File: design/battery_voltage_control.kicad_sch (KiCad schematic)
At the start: 12 parts

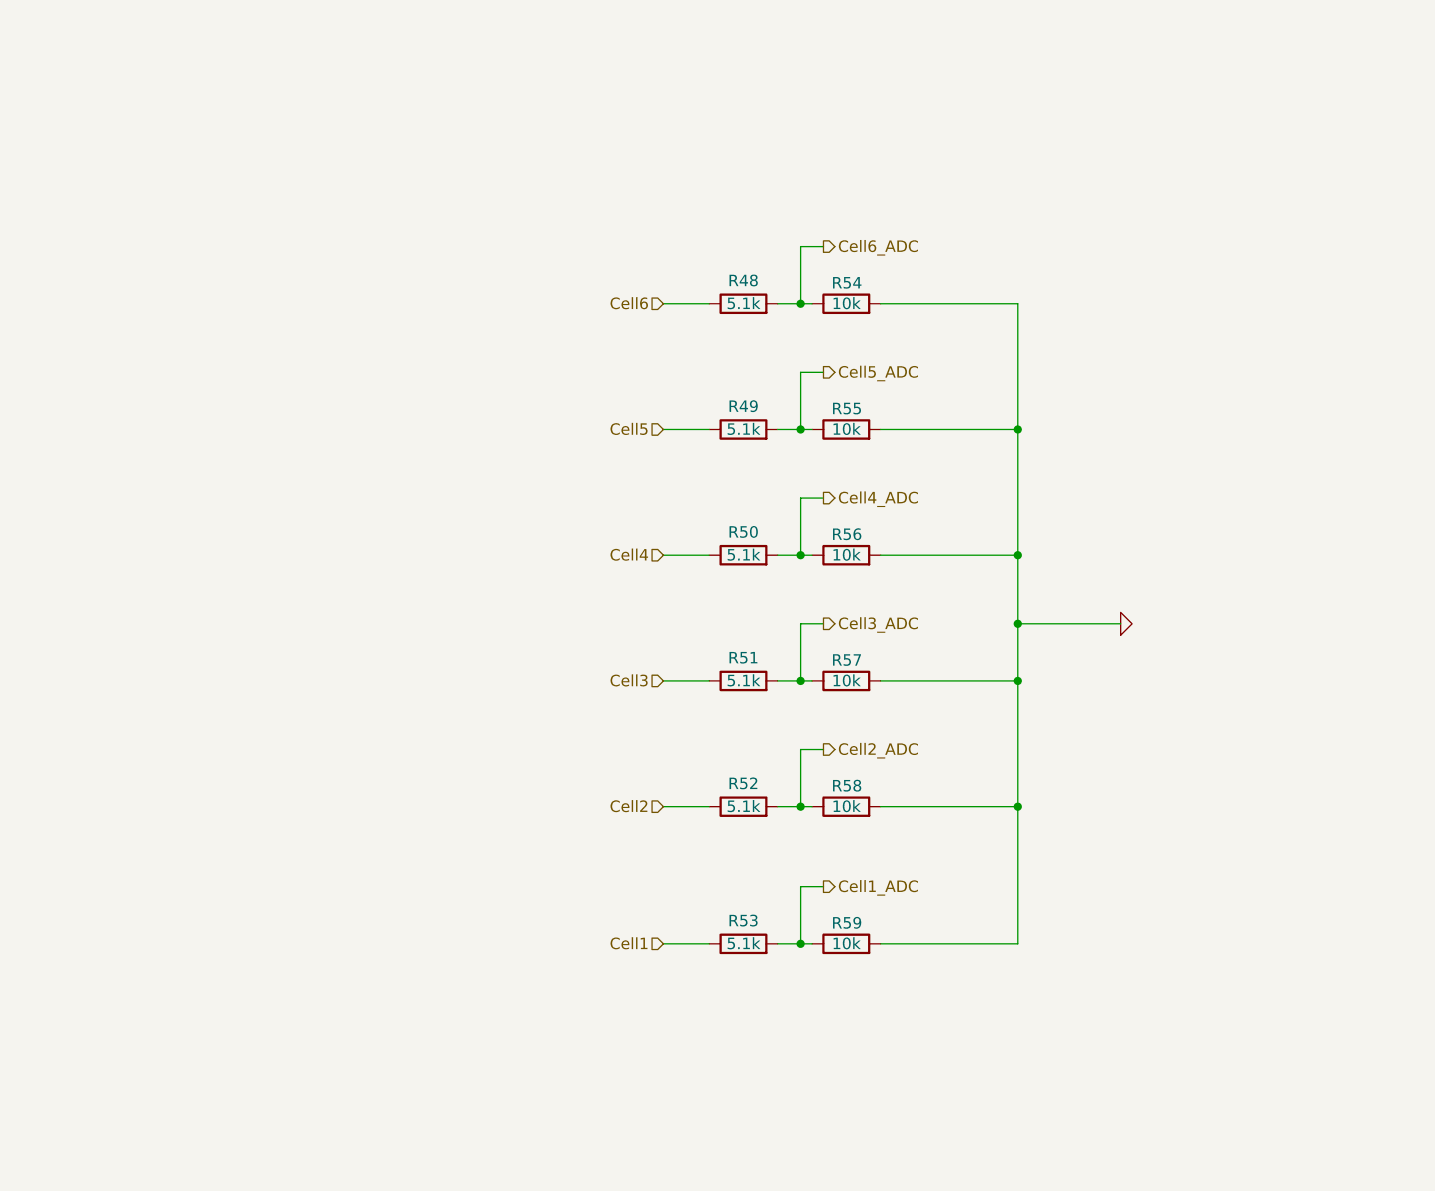
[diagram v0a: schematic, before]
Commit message: added battery balancer
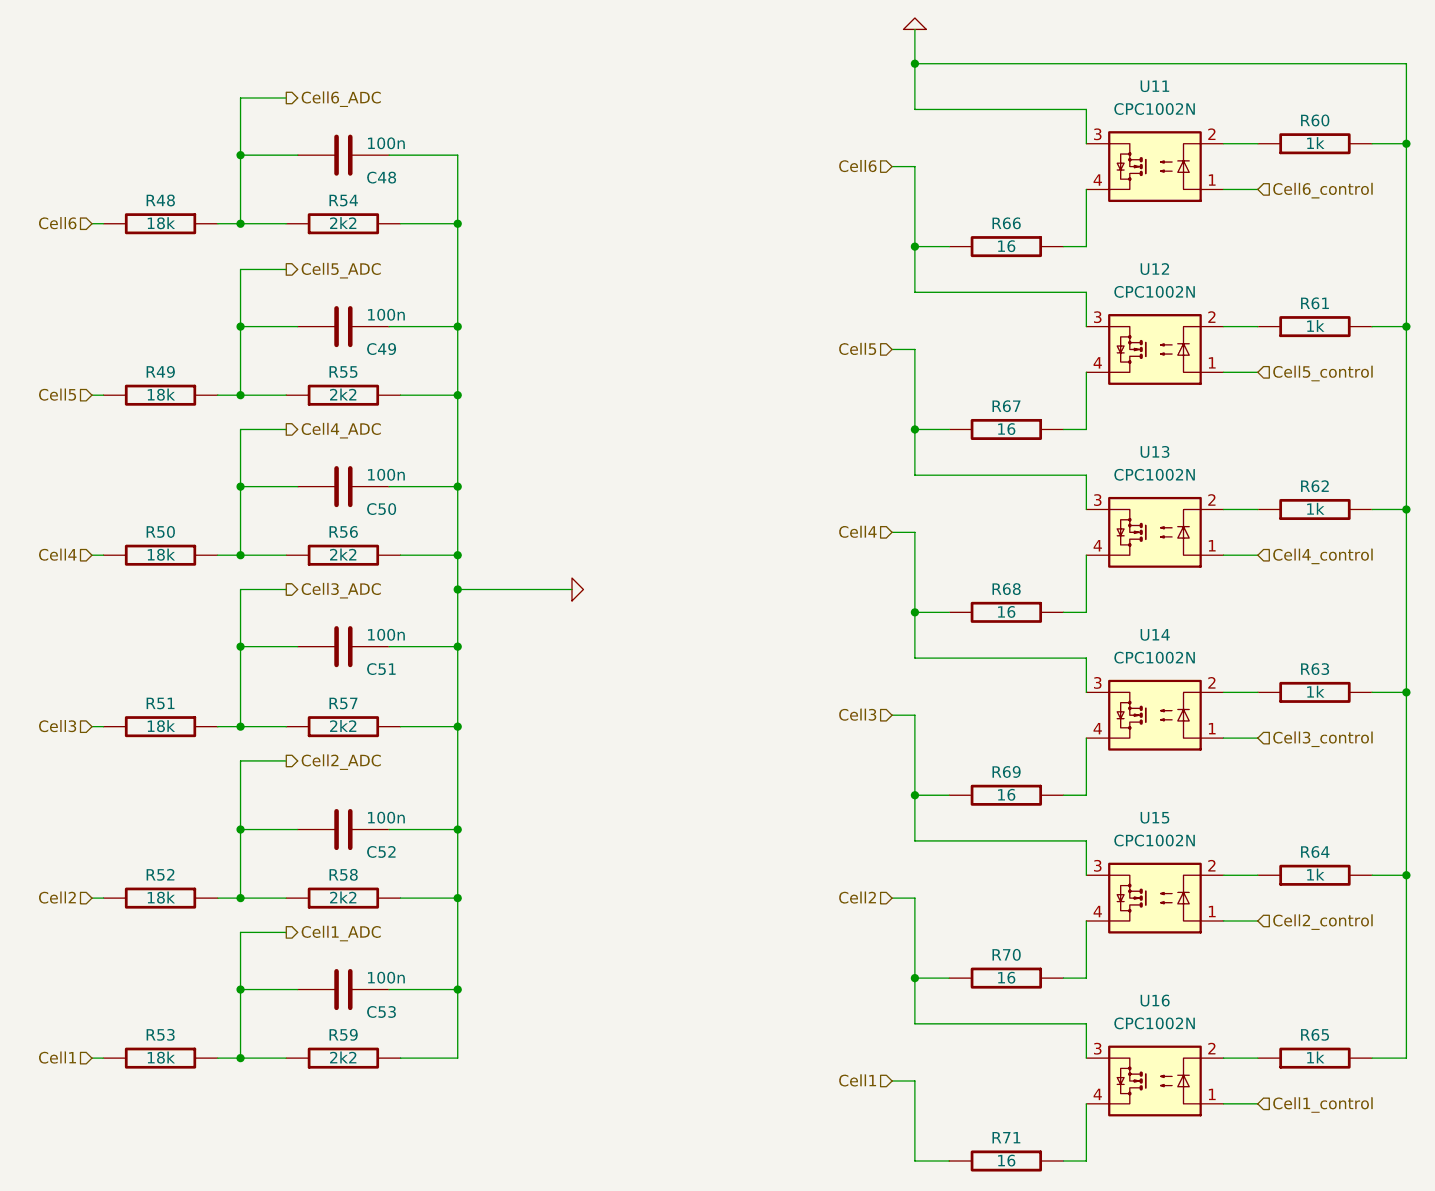
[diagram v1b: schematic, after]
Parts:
- removed R48, R49, R50, R51, R52, R53: 5.1k, CRF1:SMD-0603_r, symbol Device:R
- removed R54, R55, R56, R57, R58, R59: 10k, CRF1:SMD-0603_r, symbol Device:R
- added C48, C49, C50, C51, C52, C53: 100n, CRF1:SMD-0603_c, symbol BLDC_4-rescue:C-RESCUE-BLDC_4
- added R48, R49, R50, R51, R52, R53: 18k, CRF1:SMD-0603_r, symbol BLDC_4-rescue:R-RESCUE-BLDC_4
- added R54, R55, R56, R57, R58, R59: 2k2, CRF1:SMD-0603_r, symbol BLDC_4-rescue:R-RESCUE-BLDC_4
- added R60, R61, R62, R63, R64, R65: 1k, CRF1:SMD-0603_r, symbol BLDC_4-rescue:R-RESCUE-BLDC_4
- added R66, R67, R68, R69, R70, R71: 16, Resistor_SMD:R_2512_6332Metric, symbol BLDC_4-rescue:R-RESCUE-BLDC_4
- added U11, U12, U13, U14, U15, U16: CPC1002N, Package_SO:SOP-4_3.8x4.1mm_P2.54mm, symbol Relay_SolidState:CPC1002N
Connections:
- net Cell1: now also R53.2, R71.2
- net Cell1_ADC: now also C53.2, R53.1, R59.1
- net Cell2: now also R52.2, R70.2, U16.3
- net Cell2_ADC: now also C52.2, R52.1, R58.1
- net Cell3: now also R51.2, R69.2, U15.3
- net Cell3_ADC: now also C51.2, R51.1, R57.1
- net Cell4: now also R50.2, R68.2, U14.3
- net Cell4_ADC: now also C50.2, R50.1, R56.1
- net Cell5: now also R49.2, R67.2, U13.3
- net Cell5_ADC: now also C49.2, R49.1, R55.1
- net Cell6: now also R48.2, R66.2, U12.3
- net Cell6_ADC: now also C48.2, R48.1, R54.1
- net GND: now also C48.1, C49.1, C50.1, C51.1, C52.1, C53.1, R54.2, R55.2, R56.2, R57.2, R58.2, R59.2, R60.2, R61.2, R62.2, R63.2, R64.2, R65.2, U11.3
- new net: R64.1, U15.2
- new net: R70.1, U15.4
- new net: R69.1, U14.4
- new net: R60.1, U11.2
- new net: R66.1, U11.4
- new net: R65.1, U16.2
- new net: R71.1, U16.4
- new net: R62.1, U13.2
- new net: R68.1, U13.4
- new net: R63.1, U14.2
- new net: R67.1, U12.4
- new net: R61.1, U12.2
- new net Cell1_control: U16.1
- new net Cell2_control: U15.1
- new net Cell3_control: U14.1
- new net Cell4_control: U13.1
- new net Cell5_control: U12.1
- new net Cell6_control: U11.1

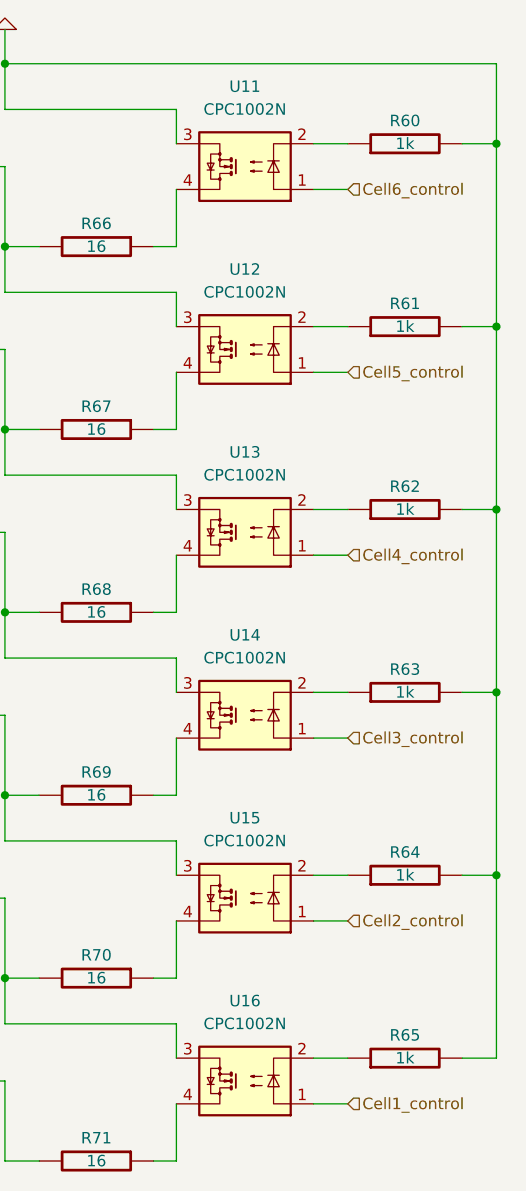
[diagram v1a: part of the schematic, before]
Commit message: change resistance for LED resistors
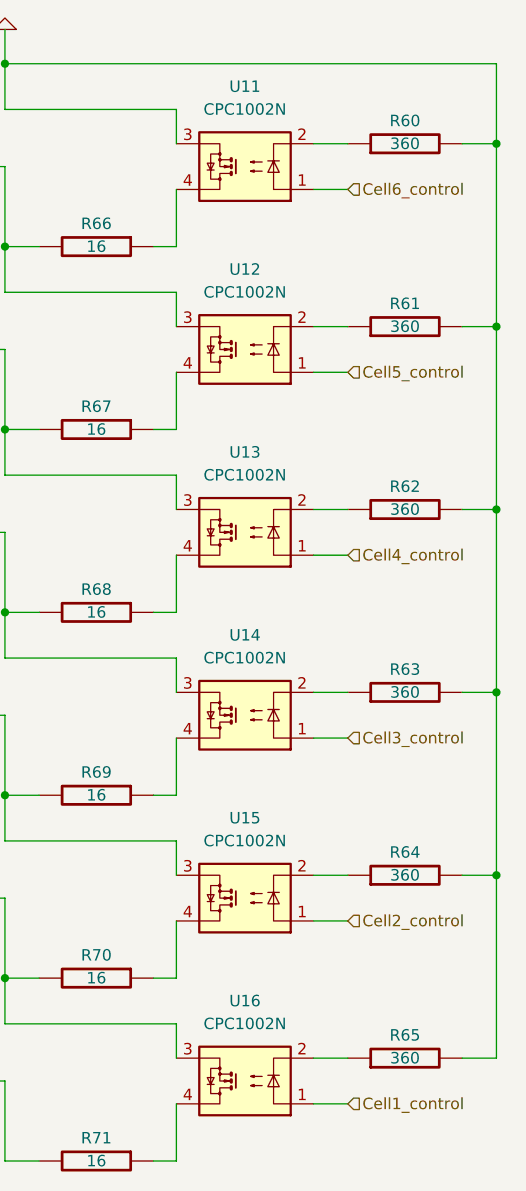
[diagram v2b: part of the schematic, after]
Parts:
- R60, R61, R62, R63, R64, R65: value 1k -> 360
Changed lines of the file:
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@@
 			)
 		)
-		(property "Value" "1k"
+		(property "Value" "360"
 			(at 198.12 118.11 90)
 			(effects
@@
 			)
 		)
-		(property "Value" "1k"
+		(property "Value" "360"
 			(at 198.12 138.43 90)
 			(effects
@@
 			)
 		)
-		(property "Value" "1k"
+		(property "Value" "360"
 			(at 198.12 36.83 90)
 			(effects
@@
 			)
 		)
-		(property "Value" "1k"
+		(property "Value" "360"
 			(at 198.12 77.47 90)
 			(effects
@@
 			)
 		)
-		(property "Value" "1k"
+		(property "Value" "360"
 			(at 198.12 97.79 90)
 			(effects
@@
 			)
 		)
-		(property "Value" "1k"
+		(property "Value" "360"
 			(at 198.12 57.15 90)
 			(effects

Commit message: added new field in components on battery balancer; pcb tracing
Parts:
- R60, R61, R62, R63, R64, R65: Код для заказа (none) -> RS-03K3600FT
- R66, R67, R68, R69, R70, R71: Код для заказа (none) -> RL2512FK-070R16L
- U11, U12, U13, U14, U15, U16: Код для заказа (none) -> CPC1002N

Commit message: added documentation
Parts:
- C48: The code for order (none) -> C1206C104K5RAC7210; Значение (none) -> 100 нФ; Наименование (none) -> Конденсатор керамический 100 нФ 0603; Обозначение (none) -> C; Позиционное обозначение (none) -> C48
- C49: The code for order (none) -> C1206C104K5RAC7210; Значение (none) -> 100 нФ; Наименование (none) -> Конденсатор керамический 100 нФ 0603; Обозначение (none) -> C; Позиционное обозначение (none) -> C49
- C50: The code for order (none) -> C1206C104K5RAC7210; Значение (none) -> 100 нФ; Наименование (none) -> Конденсатор керамический 100 нФ 0603; Обозначение (none) -> C; Позиционное обозначение (none) -> C50
- C51: The code for order (none) -> C1206C104K5RAC7210; Значение (none) -> 100 нФ; Наименование (none) -> Конденсатор керамический 100 нФ 0603; Обозначение (none) -> C; Позиционное обозначение (none) -> C51
- C52: The code for order (none) -> C1206C104K5RAC7210; Значение (none) -> 100 нФ; Наименование (none) -> Конденсатор керамический 100 нФ 0603; Обозначение (none) -> C; Позиционное обозначение (none) -> C52
- C53: The code for order (none) -> C1206C104K5RAC7210; Значение (none) -> 100 нФ; Наименование (none) -> Конденсатор керамический 100 нФ 0603; Обозначение (none) -> C; Позиционное обозначение (none) -> C53
- R48: The code for order (none) -> 18k 1% 0603; Значение (none) -> 18 кОм; Наименование (none) -> Чип резистор 18 кОм 0603 1%; Обозначение (none) -> R; Позиционное обозначение (none) -> R48
- R49: The code for order (none) -> 18k 1% 0603; Значение (none) -> 18 кОм; Наименование (none) -> Чип резистор 18 кОм 0603 1%; Обозначение (none) -> R; Позиционное обозначение (none) -> R49
- R50: The code for order (none) -> 18k 1% 0603; Значение (none) -> 18 кОм; Наименование (none) -> Чип резистор 18 кОм 0603 1%; Обозначение (none) -> R; Позиционное обозначение (none) -> R50
- R51: The code for order (none) -> 18k 1% 0603; Значение (none) -> 18 кОм; Наименование (none) -> Чип резистор 18 кОм 0603 1%; Обозначение (none) -> R; Позиционное обозначение (none) -> R51
- R52: The code for order (none) -> 18k 1% 0603; Значение (none) -> 18 кОм; Наименование (none) -> Чип резистор 18 кОм 0603 1%; Обозначение (none) -> R; Позиционное обозначение (none) -> R52
- R53: The code for order (none) -> 18k 1% 0603; Значение (none) -> 18 кОм; Наименование (none) -> Чип резистор 18 кОм 0603 1%; Обозначение (none) -> R; Позиционное обозначение (none) -> R53
- R54: The code for order (none) -> CR-03JL7---2K2; Значение (none) -> 2.2 кОм; Наименование (none) -> Чип резистор 2.2 кОм 0603 1%; Обозначение (none) -> R; Позиционное обозначение (none) -> R54
- R55: The code for order (none) -> CR-03JL7---2K2; Значение (none) -> 2.2 кОм; Наименование (none) -> Чип резистор 2.2 кОм 0603 1%; Обозначение (none) -> R; Позиционное обозначение (none) -> R55
- R56: The code for order (none) -> CR-03JL7---2K2; Значение (none) -> 2.2 кОм; Наименование (none) -> Чип резистор 2.2 кОм 0603 1%; Обозначение (none) -> R; Позиционное обозначение (none) -> R56
- R57: The code for order (none) -> CR-03JL7---2K2; Значение (none) -> 2.2 кОм; Наименование (none) -> Чип резистор 2.2 кОм 0603 1%; Обозначение (none) -> R; Позиционное обозначение (none) -> R57
- R58: The code for order (none) -> CR-03JL7---2K2; Значение (none) -> 2.2 кОм; Наименование (none) -> Чип резистор 2.2 кОм 0603 1%; Обозначение (none) -> R; Позиционное обозначение (none) -> R58
- R59: The code for order (none) -> CR-03JL7---2K2; Значение (none) -> 2.2 кОм; Наименование (none) -> Чип резистор 2.2 кОм 0603 1%; Обозначение (none) -> R; Позиционное обозначение (none) -> R59
- R60: The code for order (none) -> RS-03K3600FT; Значение (none) -> 360 Ом; Код для заказа RS-03K3600FT -> (none); Наименование (none) -> Чип резистор 360 Ом 0603 1%; Обозначение (none) -> R; Позиционное обозначение (none) -> R60
- R61: The code for order (none) -> RS-03K3600FT; Значение (none) -> 360 Ом; Код для заказа RS-03K3600FT -> (none); Наименование (none) -> Чип резистор 360 Ом 0603 1%; Обозначение (none) -> R; Позиционное обозначение (none) -> R61
- R62: The code for order (none) -> RS-03K3600FT; Значение (none) -> 360 Ом; Код для заказа RS-03K3600FT -> (none); Наименование (none) -> Чип резистор 360 Ом 0603 1%; Обозначение (none) -> R; Позиционное обозначение (none) -> R62
- R63: The code for order (none) -> RS-03K3600FT; Значение (none) -> 360 Ом; Код для заказа RS-03K3600FT -> (none); Наименование (none) -> Чип резистор 360 Ом 0603 1%; Обозначение (none) -> R; Позиционное обозначение (none) -> R63
- R64: The code for order (none) -> RS-03K3600FT; Значение (none) -> 360 Ом; Код для заказа RS-03K3600FT -> (none); Наименование (none) -> Чип резистор 360 Ом 0603 1%; Обозначение (none) -> R; Позиционное обозначение (none) -> R64
- R65: The code for order (none) -> RS-03K3600FT; Значение (none) -> 360 Ом; Код для заказа RS-03K3600FT -> (none); Наименование (none) -> Чип резистор 360 Ом 0603 1%; Обозначение (none) -> R; Позиционное обозначение (none) -> R65
- R66: The code for order (none) -> RC0603F16R; Значение (none) -> 16 Ом; Код для заказа RL2512FK-070R16L -> (none); Наименование (none) -> Чип резистор 16 Ом 2512 1%; Обозначение (none) -> R; Позиционное обозначение (none) -> R66
- R67: The code for order (none) -> RC0603F16R; Значение (none) -> 16 Ом; Код для заказа RL2512FK-070R16L -> (none); Наименование (none) -> Чип резистор 16 Ом 2512 1%; Обозначение (none) -> R; Позиционное обозначение (none) -> R67
- R68: The code for order (none) -> RC0603F16R; Значение (none) -> 16 Ом; Код для заказа RL2512FK-070R16L -> (none); Наименование (none) -> Чип резистор 16 Ом 2512 1%; Обозначение (none) -> R; Позиционное обозначение (none) -> R68
- R69: The code for order (none) -> RC0603F16R; Значение (none) -> 16 Ом; Код для заказа RL2512FK-070R16L -> (none); Наименование (none) -> Чип резистор 16 Ом 2512 1%; Обозначение (none) -> R; Позиционное обозначение (none) -> R69
- R70: The code for order (none) -> RC0603F16R; Значение (none) -> 16 Ом; Код для заказа RL2512FK-070R16L -> (none); Наименование (none) -> Чип резистор 16 Ом 2512 1%; Обозначение (none) -> R; Позиционное обозначение (none) -> R70
- R71: The code for order (none) -> RC0603F16R; Значение (none) -> 16 Ом; Код для заказа RL2512FK-070R16L -> (none); Наименование (none) -> Чип резистор 16 Ом 2512 1%; Обозначение (none) -> R; Позиционное обозначение (none) -> R71
- U11: The code for order (none) -> CPC1002N; Значение (none) -> CPC1002N; Код для заказа CPC1002N -> (none); Наименование (none) -> Опто твердотельное реле CPC1002N 0603; Обозначение (none) -> K; Позиционное обозначение (none) -> U11
- U12: The code for order (none) -> CPC1002N; Значение (none) -> CPC1002N; Код для заказа CPC1002N -> (none); Наименование (none) -> Опто твердотельное реле CPC1002N 0603; Обозначение (none) -> K; Позиционное обозначение (none) -> U12
- U13: The code for order (none) -> CPC1002N; Значение (none) -> CPC1002N; Код для заказа CPC1002N -> (none); Наименование (none) -> Опто твердотельное реле CPC1002N 0603; Обозначение (none) -> K; Позиционное обозначение (none) -> U13
- U14: The code for order (none) -> CPC1002N; Значение (none) -> CPC1002N; Код для заказа CPC1002N -> (none); Наименование (none) -> Опто твердотельное реле CPC1002N 0603; Обозначение (none) -> K; Позиционное обозначение (none) -> U14
- U15: The code for order (none) -> CPC1002N; Значение (none) -> CPC1002N; Код для заказа CPC1002N -> (none); Наименование (none) -> Опто твердотельное реле CPC1002N 0603; Обозначение (none) -> K; Позиционное обозначение (none) -> U15
- U16: The code for order (none) -> CPC1002N; Значение (none) -> CPC1002N; Код для заказа CPC1002N -> (none); Наименование (none) -> Опто твердотельное реле CPC1002N 0603; Обозначение (none) -> K; Позиционное обозначение (none) -> U16
